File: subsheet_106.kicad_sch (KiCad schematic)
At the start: 52 parts, among them P01 1K, T04 BC557B, T05 BC337-40, T06 BC547B, T07 BC547B, T08 BC557B, T09 BC547B, T10 BC547B

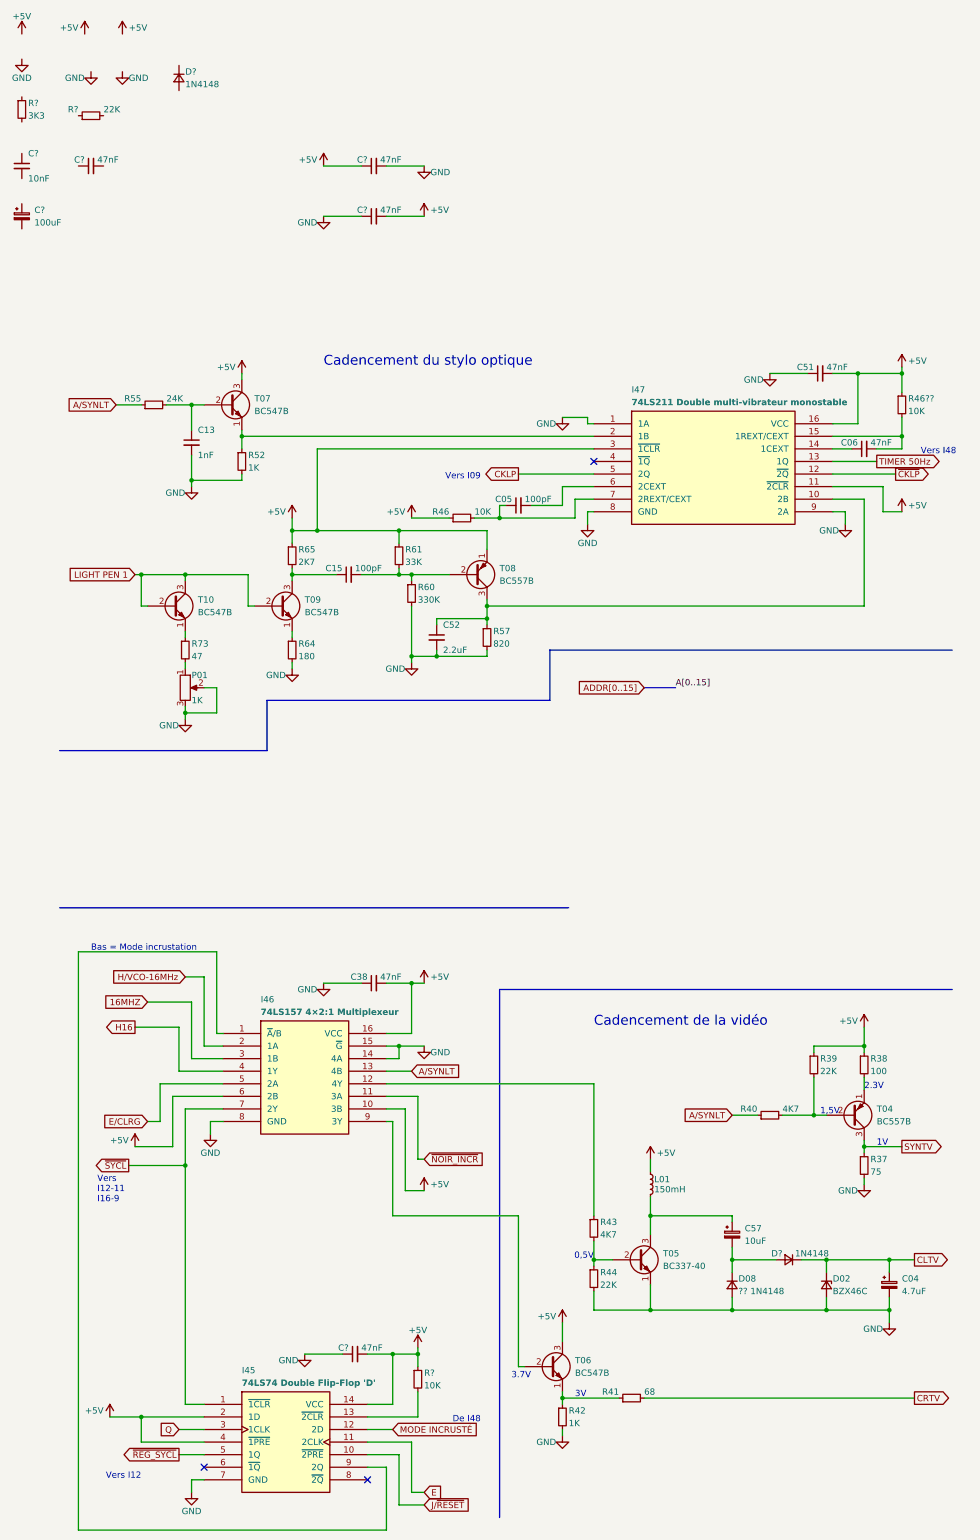
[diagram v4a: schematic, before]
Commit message: rearrange la feuille de cadencement
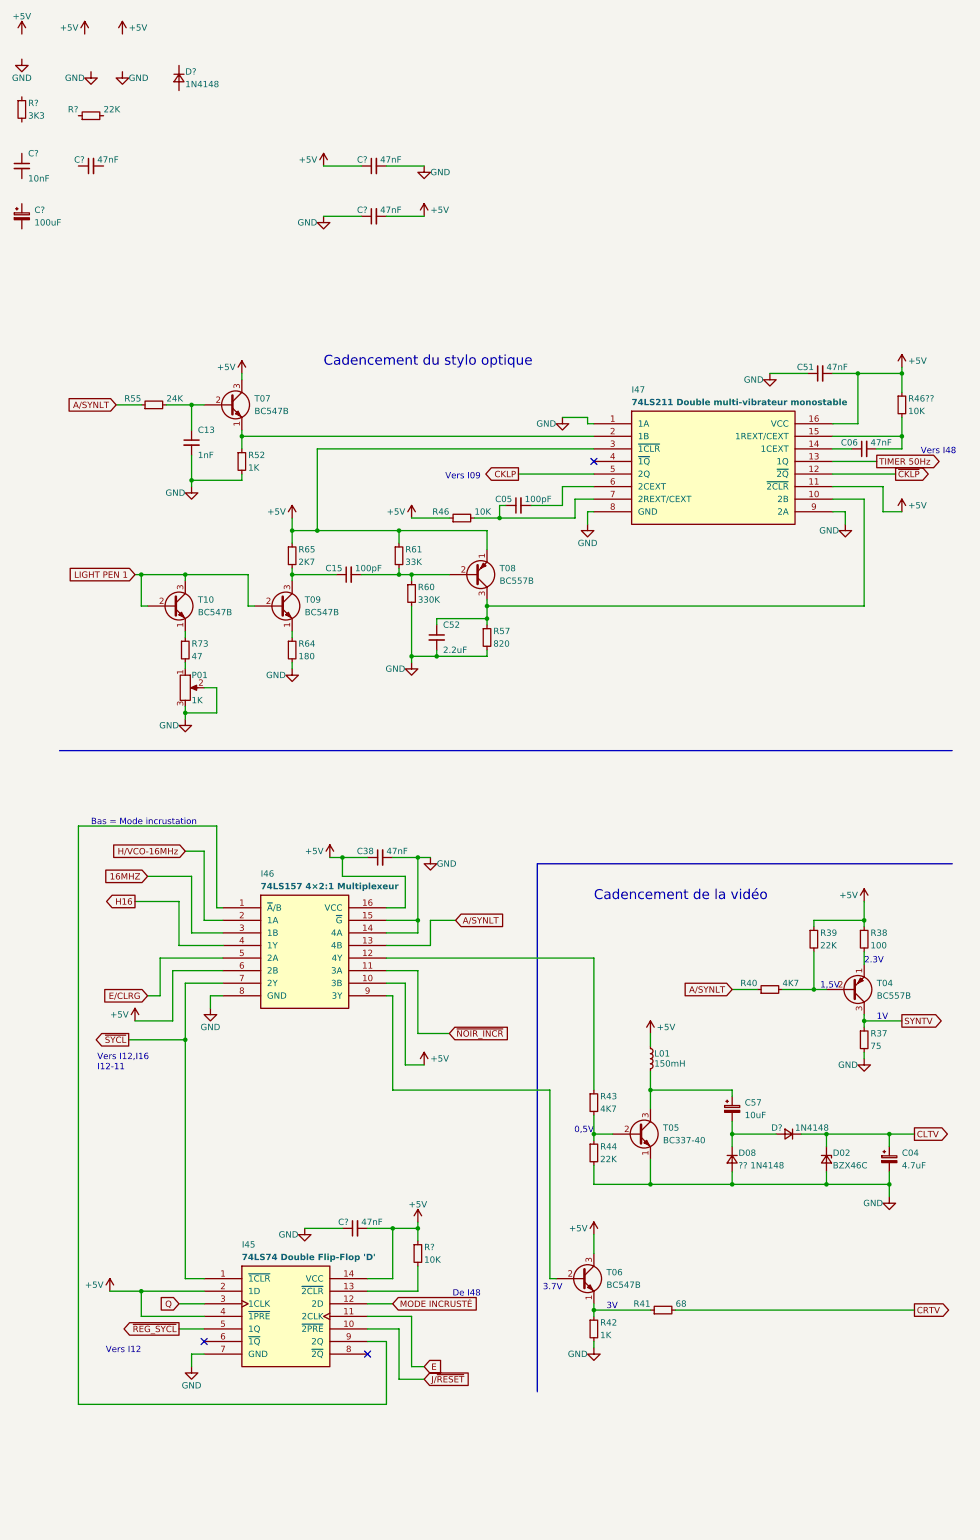
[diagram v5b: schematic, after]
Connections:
- net +5V: now also C38.1; no longer C38.2
- net GND: now also C38.2; no longer C38.1
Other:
- note added: "Vers I12,I16 I12-11"
- note removed: "Vers I12-11 I16-9"
- moved on the sheet: C04, C57, C?, D02, D08, D?, I45, I46, L01, R37, R38, R39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
